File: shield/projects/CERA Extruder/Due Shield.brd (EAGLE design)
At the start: 102.9 x 55.9 mm, 2 parts

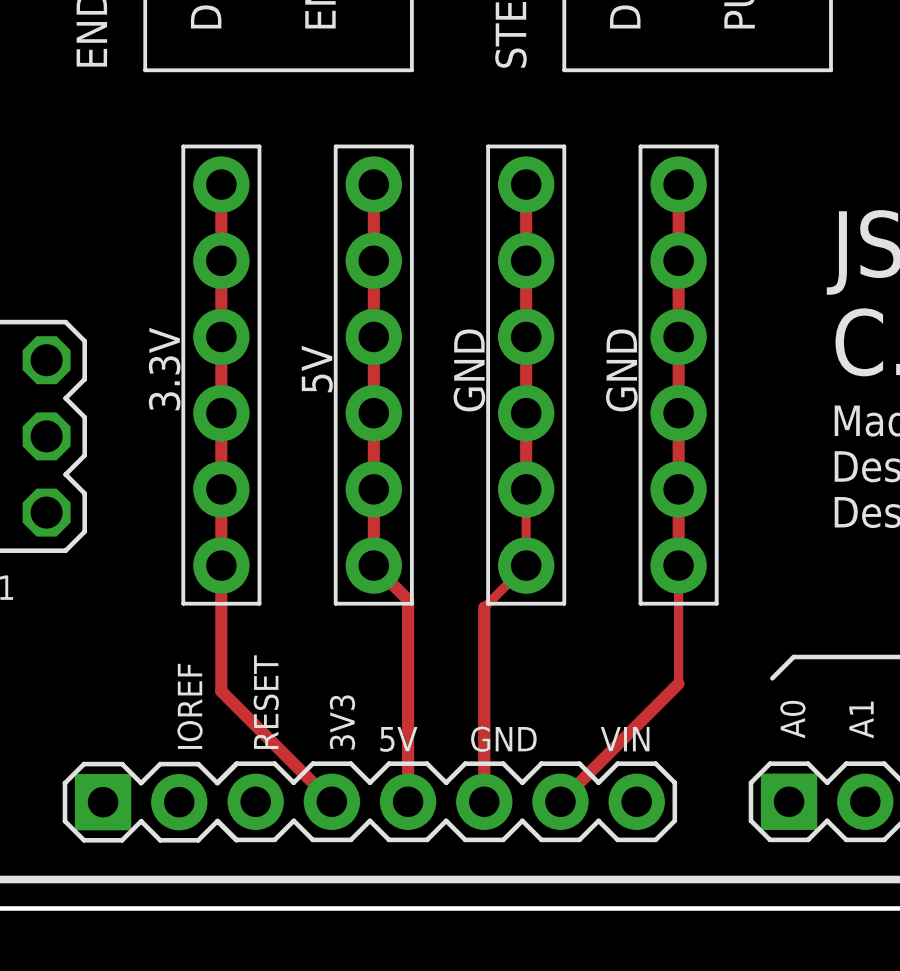
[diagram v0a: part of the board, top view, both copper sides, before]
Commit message: added loop backs
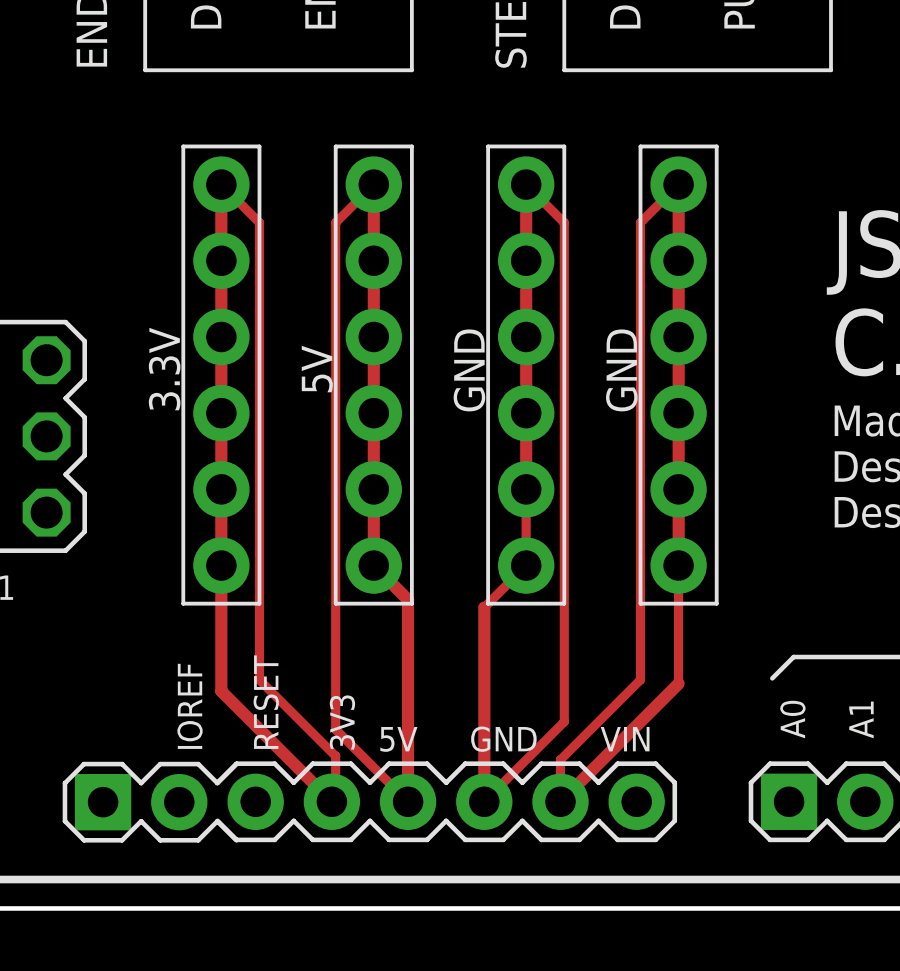
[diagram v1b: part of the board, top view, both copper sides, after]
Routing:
- net S$9: track 22.1 -> 44.3 mm
- net S$12: track 21.2 -> 43.4 mm
- net S$11: track 22.2 -> 44.4 mm
- net S$10: track 21.0 -> 43.1 mm
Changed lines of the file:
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@@
 <wire x1="31.75" y1="19.05" x2="31.75" y2="21.59" width="0.4064" layer="1"/>
 <wire x1="31.75" y1="21.59" x2="31.75" y2="24.13" width="0.4064" layer="1"/>
+<wire x1="31.75" y1="24.13" x2="33.02" y2="22.86" width="0.3048" layer="1"/>
+<wire x1="33.02" y1="22.86" x2="33.02" y2="7.62" width="0.3048" layer="1"/>
+<wire x1="33.02" y1="7.62" x2="35.56" y2="5.08" width="0.3048" layer="1"/>
+<wire x1="35.56" y1="5.08" x2="35.56" y2="3.683" width="0.3048" layer="1"/>
+<wire x1="35.56" y1="3.683" x2="35.433" y2="3.556" width="0.3048" layer="1"/>
 </signal>
 <signal name="S$10">
@@
 <wire x1="36.83" y1="11.43" x2="37.973" y2="10.287" width="0.4064" layer="1"/>
 <wire x1="37.973" y1="10.287" x2="37.973" y2="3.556" width="0.4064" layer="1"/>
+<wire x1="36.83" y1="24.13" x2="35.56" y2="22.86" width="0.3048" layer="1"/>
+<wire x1="35.56" y1="5.969" x2="37.973" y2="3.556" width="0.3048" layer="1"/>
+<wire x1="35.56" y1="22.86" x2="35.56" y2="5.969" width="0.3048" layer="1"/>
 </signal>
 <signal name="S$12">
@@
 <contactref element="E$2" pad="GND"/>
 <wire x1="40.513" y1="3.556" x2="40.513" y2="10.033" width="0.4064" layer="1"/>
+<wire x1="41.91" y1="24.13" x2="43.18" y2="22.86" width="0.3048" layer="1"/>
+<wire x1="43.18" y1="6.223" x2="40.513" y2="3.556" width="0.3048" layer="1"/>
+<wire x1="43.18" y1="22.86" x2="43.18" y2="6.223" width="0.3048" layer="1"/>
 </signal>
 <signal name="S$11">
@@
 <wire x1="46.99" y1="11.43" x2="46.99" y2="7.493" width="0.3048" layer="1"/>
 <wire x1="46.99" y1="7.493" x2="43.053" y2="3.556" width="0.4064" layer="1"/>
+<wire x1="46.99" y1="24.13" x2="45.72" y2="22.86" width="0.3048" layer="1"/>
+<wire x1="45.72" y1="22.86" x2="45.72" y2="7.62" width="0.3048" layer="1"/>
+<wire x1="43.053" y1="4.953" x2="43.053" y2="3.556" width="0.3048" layer="1"/>
+<wire x1="45.72" y1="7.62" x2="43.053" y2="4.953" width="0.3048" layer="1"/>
 </signal>
 </signals>

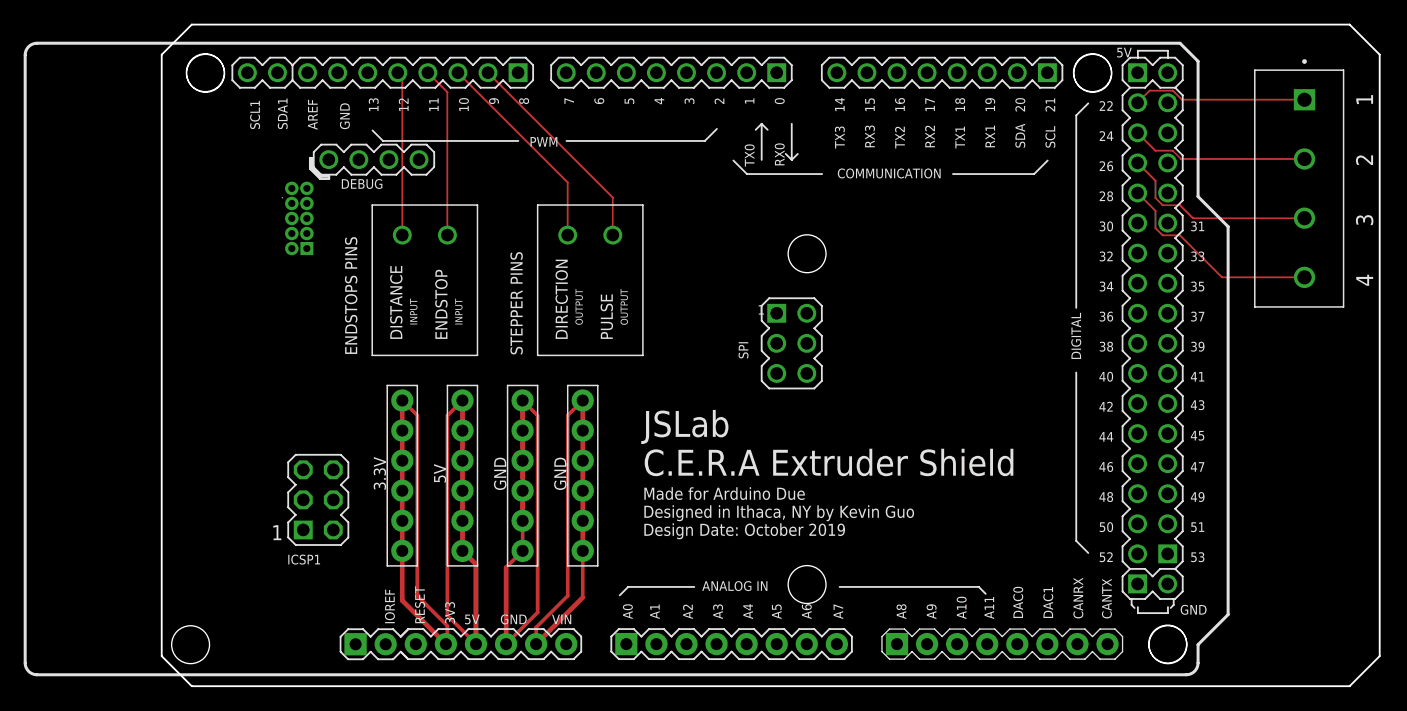
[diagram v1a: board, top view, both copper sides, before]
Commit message: made headers a proper size
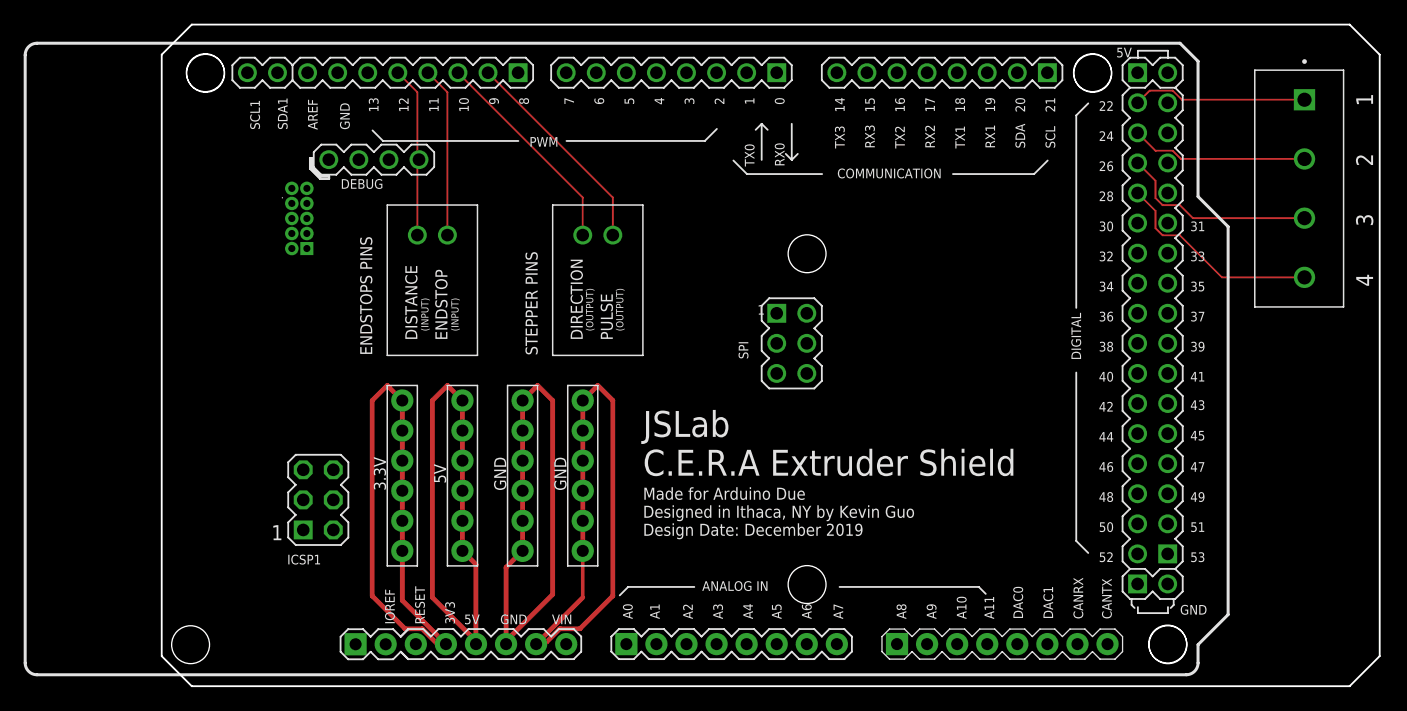
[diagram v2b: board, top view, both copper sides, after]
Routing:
- net S$9: track 44.3 -> 50.2 mm
- net S$11: track 44.4 -> 50.2 mm
- net S$10: track 43.1 -> 46.5 mm
- net S$12: track 43.4 -> 46.7 mm
- net S$2: track 17.6 -> 18.1 mm
- net S$4: track 13.9 -> 14.4 mm
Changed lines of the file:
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@@
 <contactref element="E$2" pad="DIRECTION"/>
 <contactref element="E$2" pad="10"/>
-<wire x1="45.72" y1="38.1" x2="45.72" y2="42.545" width="0.1524" layer="1"/>
-<wire x1="45.72" y1="42.545" x2="36.449" y2="51.816" width="0.1524" layer="1"/>
+<wire x1="46.99" y1="38.1" x2="46.99" y2="41.275" width="0.1524" layer="1"/>
+<wire x1="46.99" y1="41.275" x2="36.449" y2="51.816" width="0.1524" layer="1"/>
 </signal>
 <signal name="S$3">
@@
 <contactref element="E$2" pad="DIST"/>
 <contactref element="E$2" pad="12"/>
-<wire x1="31.75" y1="38.1" x2="31.75" y2="51.435" width="0.1524" layer="1"/>
-<wire x1="31.75" y1="51.435" x2="31.369" y2="51.816" width="0.1524" layer="1"/>
+<wire x1="33.02" y1="38.1" x2="33.02" y2="50.165" width="0.1524" layer="1"/>
+<wire x1="33.02" y1="50.165" x2="31.369" y2="51.816" width="0.1524" layer="1"/>
 </signal>
 <signal name="S$5">
@@
 <contactref element="E$2" pad="3V3X5"/>
 <contactref element="E$2" pad="3V3X6"/>
-<wire x1="35.433" y1="3.556" x2="31.75" y2="7.239" width="0.4064" layer="1"/>
+<wire x1="35.433" y1="3.556" x2="35.3695" y2="3.6195" width="0.4064" layer="1"/>
+<wire x1="35.3695" y1="3.6195" x2="31.75" y2="7.239" width="0.4064" layer="1"/>
 <wire x1="31.75" y1="7.239" x2="31.75" y2="11.43" width="0.4064" layer="1"/>
 <wire x1="31.75" y1="11.43" x2="31.75" y2="13.97" width="0.4064" layer="1"/>
@@
 <wire x1="31.75" y1="19.05" x2="31.75" y2="21.59" width="0.4064" layer="1"/>
 <wire x1="31.75" y1="21.59" x2="31.75" y2="24.13" width="0.4064" layer="1"/>
-<wire x1="31.75" y1="24.13" x2="33.02" y2="22.86" width="0.3048" layer="1"/>
-<wire x1="33.02" y1="22.86" x2="33.02" y2="7.62" width="0.3048" layer="1"/>
-<wire x1="33.02" y1="7.62" x2="35.56" y2="5.08" width="0.3048" layer="1"/>
-<wire x1="35.56" y1="5.08" x2="35.56" y2="3.683" width="0.3048" layer="1"/>
 <wire x1="35.56" y1="3.683" x2="35.433" y2="3.556" width="0.3048" layer="1"/>
+<wire x1="31.75" y1="24.13" x2="30.48" y2="25.4" width="0.4064" layer="1"/>
+<wire x1="30.48" y1="25.4" x2="29.21" y2="24.13" width="0.4064" layer="1"/>
+<wire x1="29.21" y1="24.13" x2="29.21" y2="7.62" width="0.4064" layer="1"/>
+<wire x1="29.21" y1="7.62" x2="31.9796" y2="4.8504" width="0.4064" layer="1"/>
+<wire x1="34.660475" y1="3.6195" x2="35.3695" y2="3.6195" width="0.4064" layer="1"/>
+<wire x1="31.9796" y1="4.8504" x2="33.429575" y2="4.8504" width="0.4064" layer="1"/>
+<wire x1="33.429575" y1="4.8504" x2="34.660475" y2="3.6195" width="0.4064" layer="1"/>
 </signal>
 <signal name="S$10">
@@
 <wire x1="36.83" y1="13.97" x2="36.83" y2="11.43" width="0.4064" layer="1"/>
 <wire x1="36.83" y1="11.43" x2="37.973" y2="10.287" width="0.4064" layer="1"/>
-<wire x1="37.973" y1="10.287" x2="37.973" y2="3.556" width="0.4064" layer="1"/>
-<wire x1="36.83" y1="24.13" x2="35.56" y2="22.86" width="0.3048" layer="1"/>
-<wire x1="35.56" y1="5.969" x2="37.973" y2="3.556" width="0.3048" layer="1"/>
-<wire x1="35.56" y1="22.86" x2="35.56" y2="5.969" width="0.3048" layer="1"/>
+<wire x1="37.973" y1="10.287" x2="37.973" y2="3.81" width="0.4064" layer="1"/>
+<wire x1="37.973" y1="3.81" x2="37.973" y2="3.556" width="0.4064" layer="1"/>
+<wire x1="36.83" y1="24.13" x2="35.56" y2="25.4" width="0.4064" layer="1"/>
+<wire x1="35.56" y1="25.4" x2="34.29" y2="24.13" width="0.4064" layer="1"/>
+<wire x1="34.29" y1="24.13" x2="34.29" y2="7.493" width="0.4064" layer="1"/>
+<wire x1="34.29" y1="7.493" x2="37.973" y2="3.81" width="0.4064" layer="1"/>
 </signal>
 <signal name="S$12">
@@
 <wire x1="41.91" y1="16.51" x2="41.91" y2="13.97" width="0.4064" layer="1"/>
 <contactref element="E$2" pad="GNDX1"/>
-<wire x1="41.91" y1="11.43" x2="41.91" y2="13.97" width="0.3048" layer="1"/>
-<wire x1="40.513" y1="10.033" x2="41.91" y2="11.43" width="0.3048" layer="1"/>
+<wire x1="41.91" y1="11.43" x2="41.91" y2="13.97" width="0.4064" layer="1"/>
+<wire x1="40.513" y1="10.033" x2="41.91" y2="11.43" width="0.4064" layer="1"/>
 <contactref element="E$2" pad="GND"/>
-<wire x1="40.513" y1="3.556" x2="40.513" y2="10.033" width="0.4064" layer="1"/>
-<wire x1="41.91" y1="24.13" x2="43.18" y2="22.86" width="0.3048" layer="1"/>
-<wire x1="43.18" y1="6.223" x2="40.513" y2="3.556" width="0.3048" layer="1"/>
-<wire x1="43.18" y1="22.86" x2="43.18" y2="6.223" width="0.3048" layer="1"/>
+<wire x1="40.513" y1="3.556" x2="40.513" y2="3.81" width="0.4064" layer="1"/>
+<wire x1="40.513" y1="3.81" x2="40.513" y2="10.033" width="0.4064" layer="1"/>
+<wire x1="41.91" y1="24.13" x2="43.18" y2="25.4" width="0.4064" layer="1"/>
+<wire x1="43.18" y1="25.4" x2="44.45" y2="24.13" width="0.4064" layer="1"/>
+<wire x1="44.45" y1="24.13" x2="44.45" y2="7.747" width="0.4064" layer="1"/>
+<wire x1="44.45" y1="7.747" x2="40.513" y2="3.81" width="0.4064" layer="1"/>
 </signal>
 <signal name="S$11">
@@
 <contactref element="E$2" pad="GND_1"/>
 <wire x1="46.99" y1="11.43" x2="46.99" y2="7.493" width="0.3048" layer="1"/>
-<wire x1="46.99" y1="7.493" x2="43.053" y2="3.556" width="0.4064" layer="1"/>
-<wire x1="46.99" y1="24.13" x2="45.72" y2="22.86" width="0.3048" layer="1"/>
-<wire x1="45.72" y1="22.86" x2="45.72" y2="7.62" width="0.3048" layer="1"/>
-<wire x1="43.053" y1="4.953" x2="43.053" y2="3.556" width="0.3048" layer="1"/>
-<wire x1="45.72" y1="7.62" x2="43.053" y2="4.953" width="0.3048" layer="1"/>
+<wire x1="46.99" y1="7.493" x2="43.2435" y2="3.7465" width="0.4064" layer="1"/>
+<wire x1="43.2435" y1="3.7465" x2="43.053" y2="3.556" width="0.4064" layer="1"/>
+<wire x1="46.99" y1="24.13" x2="48.26" y2="25.4" width="0.4064" layer="1"/>
+<wire x1="48.26" y1="25.4" x2="49.53" y2="24.13" width="0.4064" layer="1"/>
+<wire x1="49.53" y1="24.13" x2="49.53" y2="7.62" width="0.4064" layer="1"/>
+<wire x1="49.53" y1="7.62" x2="46.7614" y2="4.8514" width="0.4064" layer="1"/>
+<wire x1="43.951525" y1="3.7465" x2="43.2435" y2="3.7465" width="0.4064" layer="1"/>
+<wire x1="46.7614" y1="4.8514" x2="45.056425" y2="4.8514" width="0.4064" layer="1"/>
+<wire x1="45.056425" y1="4.8514" x2="43.951525" y2="3.7465" width="0.4064" layer="1"/>
 </signal>
 </signals>
